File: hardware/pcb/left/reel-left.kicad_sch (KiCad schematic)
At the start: 48 parts, among them J1 Conn_01x02, SW1 SW_Push, SW10 SW_Push, SW11 SW_Push, SW12 SW_Push, SW13 SW_Push, SW14 SW_Push, SW15 SW_Push, SW16 SW_Push, SW17 SW_Push, SW18 SW_Push, SW19 SW_Push, SW2 SW_Push, SW20 SW_Push, SW21 SW_Push, SW22 SW_Push, SW24 SW_SPDT, SW25 RotaryEncoder, SW3 SW_Push, SW4 SW_Push, SW5 SW_Push, SW6 SW_Push, SW7 SW_Push, SW8 SW_Push, SW9 SW_Push

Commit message: Update PCB layouts and mechanical assets
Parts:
- added J2: Conn_01x05, reel:Display_BeeKeeb_MIP_1.08in_LS011B7DH03, symbol Connector_Generic:Conn_01x05
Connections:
- net GND: now also J2.1 (Pin_1)
- net 3.3V: now reaches U1.12 (3V3)
- net 3.3V: now also J2.2 (Pin_2)
- net SI: now reaches U1.17 (NFC3_0.16)
- net SI: now also J2.3 (Pin_3)
- net SCK: now reaches U1.18 (NFC4_1.00)
- net SCK: now also J2.4 (Pin_4)
- net CS: now reaches U1.19 (NFC5_1.10)
- net CS: now also J2.5 (Pin_5)
- no-connect marks 7 -> 4

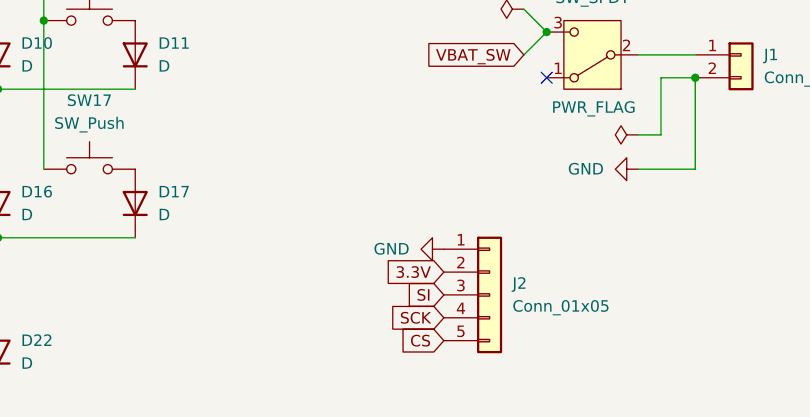
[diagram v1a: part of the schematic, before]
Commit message: Correct ReeL PCB connector pinouts and routing
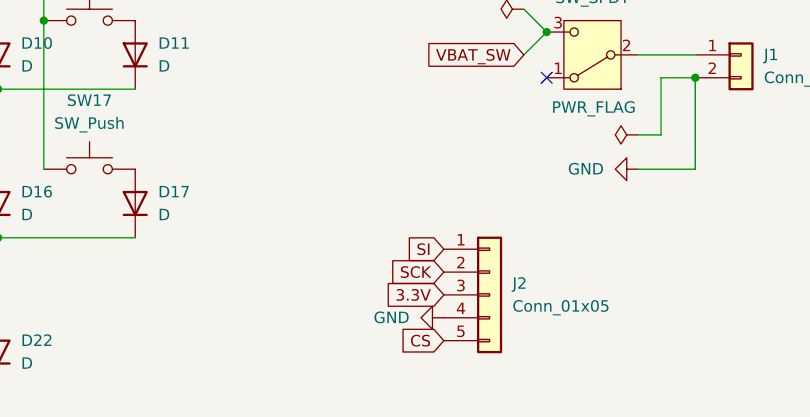
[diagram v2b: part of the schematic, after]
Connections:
- net 3.3V: now also J2.3 (Pin_3); no longer J2.2 (Pin_2)
- net GND: now also J2.4 (Pin_4); no longer J2.1 (Pin_1)
- net SCK: now also J2.2 (Pin_2); no longer J2.4 (Pin_4)
- net SI: now also J2.1 (Pin_1); no longer J2.3 (Pin_3)
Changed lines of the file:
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@@
 	(global_label "SCK"
 		(shape input)
-		(at 152.4 154.94 180)
+		(at 152.4 149.86 180)
 		(fields_autoplaced yes)
 		(effects
@@
 		)
 		(property "Intersheetrefs" "${INTERSHEET_REFS}"
-			(at 145.6653 154.94 0)
+			(at 145.6653 149.86 0)
 			(hide yes)
 			(show_name no)
@@
 	(global_label "SI"
 		(shape input)
-		(at 152.4 152.4 180)
+		(at 152.4 147.32 180)
 		(fields_autoplaced yes)
 		(effects
@@
 		)
 		(property "Intersheetrefs" "${INTERSHEET_REFS}"
-			(at 147.6005 152.4 0)
+			(at 147.6005 147.32 0)
 			(hide yes)
 			(show_name no)
@@
 	(global_label "3.3V"
 		(shape input)
-		(at 152.4 149.86 180)
+		(at 152.4 152.4 180)
 		(fields_autoplaced yes)
 		(effects
@@
 		)
 		(property "Intersheetrefs" "${INTERSHEET_REFS}"
-			(at 145.3024 149.86 0)
+			(at 145.3024 152.4 0)
 			(hide yes)
 			(show_name no)
@@
 	(symbol
 		(lib_id "power:GND")
-		(at 152.4 147.32 270)
+		(at 152.4 154.94 270)
 		(unit 1)
 		(body_style 1)
@@
 		(fields_autoplaced yes)
 		(property "Reference" "#PWR03"
-			(at 146.05 147.32 0)
+			(at 146.05 154.94 0)
 			(hide yes)
 			(show_name no)
@@
 		)
 		(property "Value" "GND"
-			(at 148.59 147.3199 90)
+			(at 148.59 154.9399 90)
 			(show_name no)
 			(do_not_autoplace no)
@@
 		)
 		(property "Footprint" ""
-			(at 152.4 147.32 0)
+			(at 152.4 154.94 0)
 			(hide yes)
 			(show_name no)
@@
 		)
 		(property "Datasheet" ""
-			(at 152.4 147.32 0)
+			(at 152.4 154.94 0)
 			(hide yes)
 			(show_name no)
@@
 		)
 		(property "Description" "Power symbol creates a global label with name \"GND\" , ground"
-			(at 152.4 147.32 0)
-			(hide yes)
-			(show_name no)
+			(at 152.4 154.94 0)
+			(hide yes)
+			(show_name no)
